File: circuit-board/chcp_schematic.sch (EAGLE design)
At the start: 18 parts, among them IC1 ATMEGA168-20P, IC2 24MAC402-SSHM-T, Q1 16 MHz

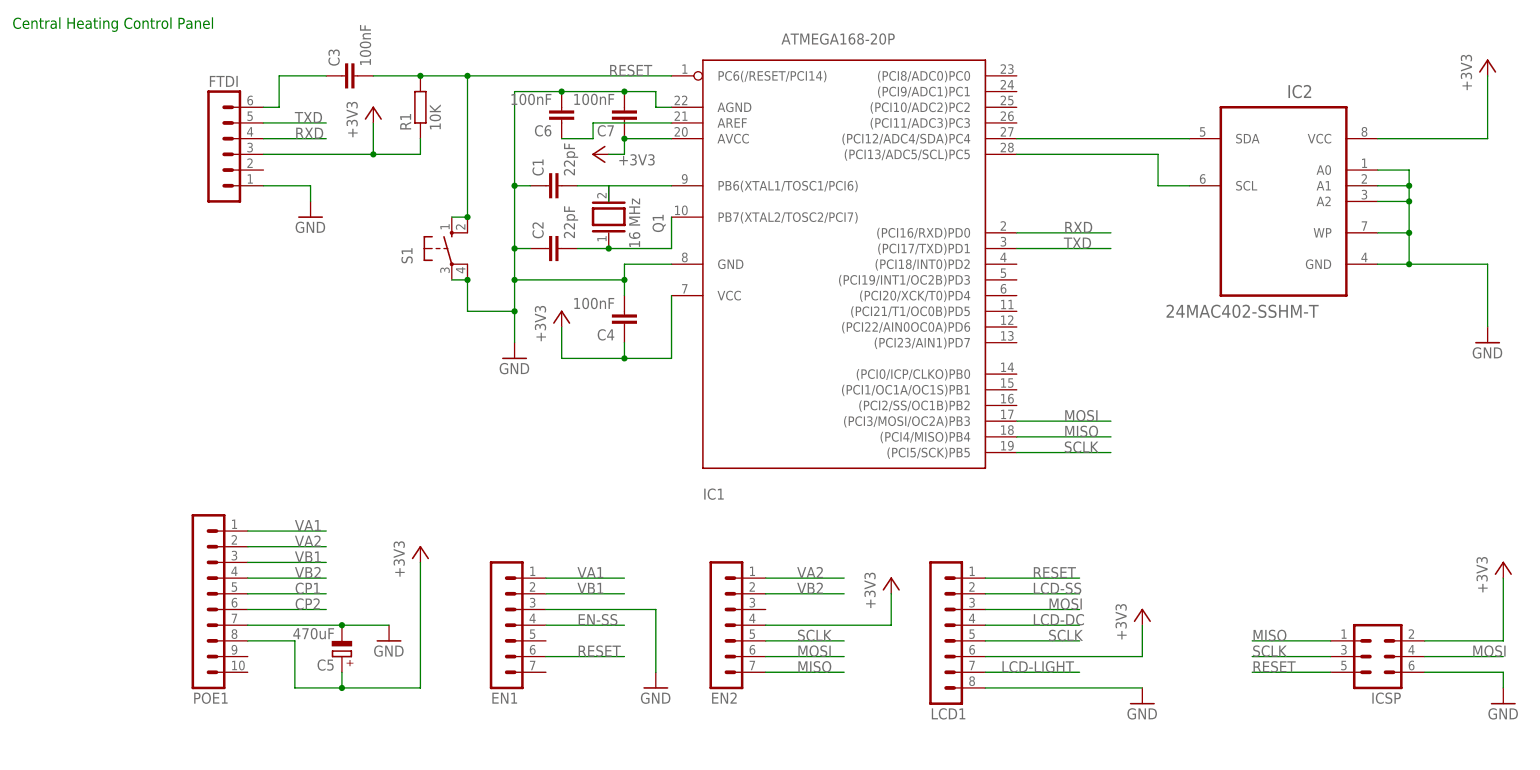
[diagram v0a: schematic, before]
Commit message: Made custom parts for the modules instead of using headers
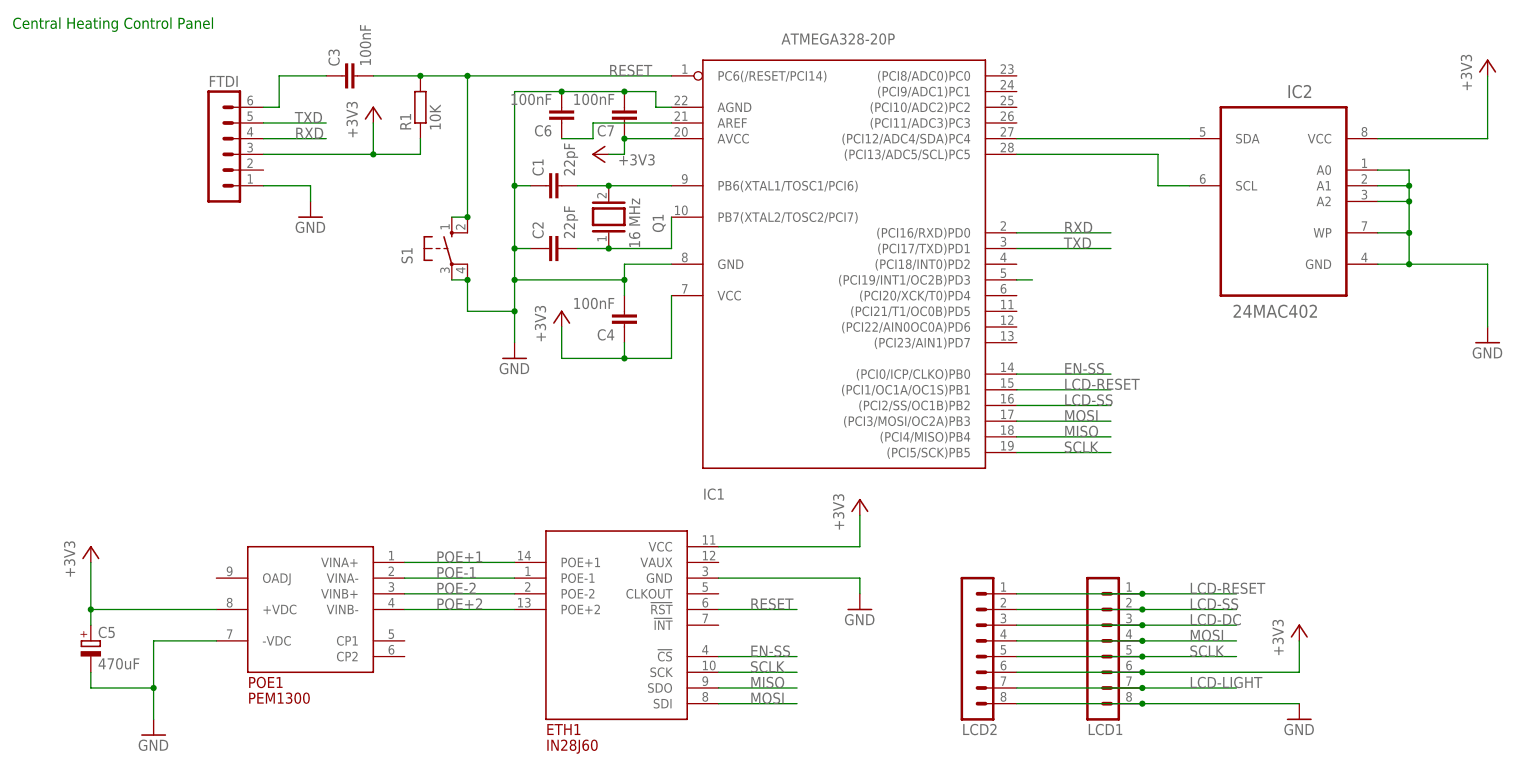
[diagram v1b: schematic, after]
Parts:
- removed EN1, EN2: (no value), con-lstb:MA07-1
- removed ICSP: (no value), con-lstb:MA03-2
- added ETH1: IN28J60, in28j60:IN28J60
- added LCD2: (no value), con-lstb:MA08-1
- IC1: value ATMEGA168-20P -> ATMEGA328-20P; device adafruit:ATMEGA168-20P -> atmega328:ATMEGA328-20P
- IC2: value 24MAC402-SSHM-T -> 24MAC402; device atmel-24mac402:24MAC402-SSHM-T -> at24mac402:24MAC402-SSHM-TPDIP
- POE1: value (none) -> PEM1300; device con-lstb:MA10-1 -> pem1300:PEM1300
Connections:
- removed net CP1: POE1.5
- removed net CP2: POE1.6
- removed net N$1 (its old number): C1.2, Q1.2
- removed net VA1: EN1.1, POE1.1
- removed net VA2: EN2.1, POE1.2
- removed net VB1: EN1.2, POE1.3
- removed net VB2: EN2.2, POE1.4
- new net LCD-RESET: IC1.(PCI1/OC1A/OC1S)PB1, LCD1.1, LCD2.1
- new net N$8: IC1.(PCI19/INT1/OC2B)PD3
- new net POE+1: ETH1.POE+1, POE1.VINA+
- new net POE+2: ETH1.POE+2, POE1.VINB-
- new net POE-1: ETH1.POE-1, POE1.VINA-
- new net POE-2: ETH1.POE-2, POE1.VINB+
- net +3V3: now also ETH1.VCC, LCD2.6, POE1.+VDC; no longer EN2.4, ICSP.2, POE1.8
- net EN-SS: now also ETH1.!CS!, IC1.(PCI0/ICP/CLKO)PB0; no longer EN1.4
- net GND: now also ETH1.GND, LCD2.8, POE1.-VDC; no longer EN1.3, ICSP.6, POE1.7
- net LCD-DC: now also LCD1.3, LCD2.3; no longer LCD1.4
- net LCD-LIGHT: now also LCD2.7
- net LCD-SS: now also IC1.(PCI2/SS/OC1B)PB2, LCD2.2
- net MISO: now also ETH1.SDO; no longer EN2.7, ICSP.1
- net MOSI: now also ETH1.SDI, LCD1.4, LCD2.4; no longer EN2.6, ICSP.4, LCD1.3
- net N$6: now also C1.2, Q1.2
- net RESET: now also ETH1.!RST!; no longer EN1.6, ICSP.5, LCD1.1
- net SCLK: now also ETH1.SCK, LCD2.5; no longer EN2.5, ICSP.3
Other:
- moved on the sheet: C5, LCD1

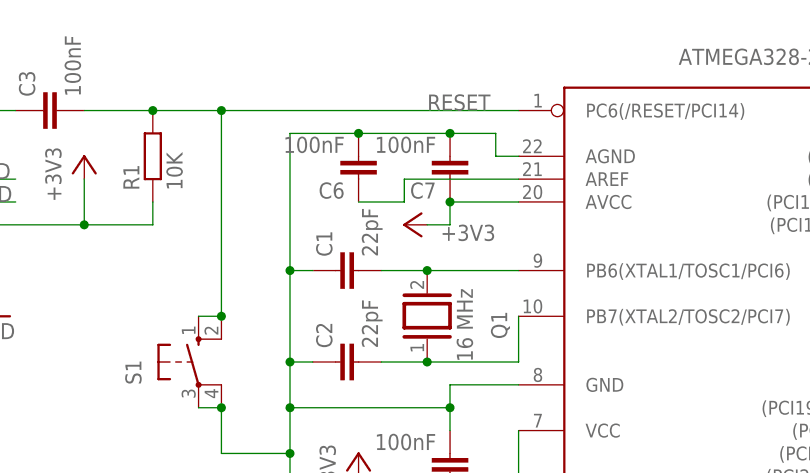
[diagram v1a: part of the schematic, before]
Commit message: Removed the unnecessary capacitor connected to AREF
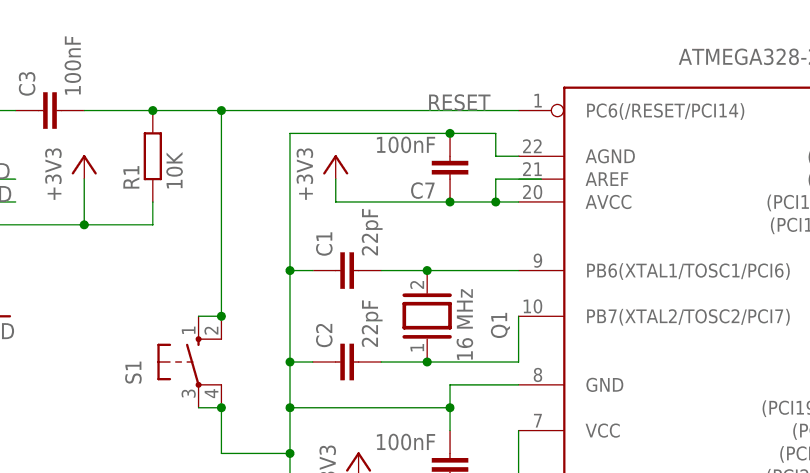
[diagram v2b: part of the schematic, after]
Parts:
- removed C6: 100nF, rcl:C-EU025-024X044
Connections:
- removed net N$7: C6.1, IC1.AREF
- net GND: no longer C6.2
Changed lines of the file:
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@@
 <part name="R1" library="rcl" deviceset="R-EU_" device="0204/7" value="10K"/>
 <part name="S1" library="switch-omron" deviceset="10-XX" device=""/>
-<part name="C6" library="rcl" deviceset="C-EU" device="025-024X044" value="100nF"/>
 <part name="C7" library="rcl" deviceset="C-EU" device="025-024X044" value="100nF"/>
 <part name="+3V8" library="supply1" deviceset="+3V3" device=""/>
@@
 <instance part="R1" gate="G$1" x="-66.04" y="55.88" rot="R90"/>
 <instance part="S1" gate="1" x="-60.96" y="33.02"/>
-<instance part="C6" gate="G$1" x="-43.18" y="53.34" rot="R180"/>
 <instance part="C7" gate="G$1" x="-33.02" y="53.34" rot="R180"/>
-<instance part="+3V8" gate="G$1" x="-38.1" y="48.26" smashed="yes" rot="R90">
-<attribute name="VALUE" x="-27.94" y="48.26" size="1.778" layer="96" rot="R180"/>
+<instance part="+3V8" gate="G$1" x="-45.72" y="55.88" smashed="yes">
+<attribute name="VALUE" x="-48.26" y="50.8" size="1.778" layer="96" rot="R90"/>
 </instance>
 <instance part="POE1" gate="G$1" x="-83.82" y="-25.4"/>
@@
 <segment>
 <pinref part="+3V8" gate="G$1" pin="+3V3"/>
-<wire x1="-35.56" y1="48.26" x2="-33.02" y2="48.26" width="0.1524" layer="91"/>
+<wire x1="-45.72" y1="53.34" x2="-45.72" y2="50.8" width="0.1524" layer="91"/>
 <pinref part="C7" gate="G$1" pin="1"/>
 <pinref part="IC1" gate="G$1" pin="AVCC"/>
-<wire x1="-25.4" y1="50.8" x2="-33.02" y2="50.8" width="0.1524" layer="91"/>
-<wire x1="-33.02" y1="48.26" x2="-33.02" y2="50.8" width="0.1524" layer="91"/>
+<wire x1="-25.4" y1="50.8" x2="-27.94" y2="50.8" width="0.1524" layer="91"/>
+<wire x1="-27.94" y1="50.8" x2="-33.02" y2="50.8" width="0.1524" layer="91"/>
+<wire x1="-45.72" y1="50.8" x2="-33.02" y2="50.8" width="0.1524" layer="91"/>
 <junction x="-33.02" y="50.8"/>
+<wire x1="-22.86" y1="53.34" x2="-27.94" y2="53.34" width="0.1524" layer="91"/>
+<wire x1="-27.94" y1="53.34" x2="-27.94" y2="50.8" width="0.1524" layer="91"/>
+<junction x="-27.94" y="50.8"/>
 </segment>
 </net>
@@
 <pinref part="GND1" gate="1" pin="GND"/>
 <wire x1="-50.8" y1="17.78" x2="-50.8" y2="22.86" width="0.1524" layer="91"/>
-<wire x1="-43.18" y1="58.42" x2="-50.8" y2="58.42" width="0.1524" layer="91"/>
 <wire x1="-50.8" y1="58.42" x2="-50.8" y2="43.18" width="0.1524" layer="91"/>
 <pinref part="C1" gate="G$1" pin="1"/>
@@
 <wire x1="-58.42" y1="22.86" x2="-50.8" y2="22.86" width="0.1524" layer="91"/>
 <junction x="-50.8" y="22.86"/>
-<pinref part="C6" gate="G$1" pin="2"/>
 <pinref part="IC1" gate="G$1" pin="AGND"/>
 <wire x1="-25.4" y1="55.88" x2="-27.94" y2="55.88" width="0.1524" layer="91"/>
 <wire x1="-27.94" y1="55.88" x2="-27.94" y2="58.42" width="0.1524" layer="91"/>
 <wire x1="-27.94" y1="58.42" x2="-33.02" y2="58.42" width="0.1524" layer="91"/>
-<junction x="-43.18" y="58.42"/>
 <pinref part="C7" gate="G$1" pin="2"/>
-<wire x1="-33.02" y1="58.42" x2="-43.18" y2="58.42" width="0.1524" layer="91"/>
+<wire x1="-33.02" y1="58.42" x2="-50.8" y2="58.42" width="0.1524" layer="91"/>
 <junction x="-33.02" y="58.42"/>
 <pinref part="C4" gate="G$1" pin="2"/>
@@
 </segment>
 </net>
-<net name="N$7" class="0">
-<segment>
-<wire x1="-38.1" y1="50.8" x2="-38.1" y2="53.34" width="0.1524" layer="91"/>
-<pinref part="IC1" gate="G$1" pin="AREF"/>
-<wire x1="-38.1" y1="53.34" x2="-25.4" y2="53.34" width="0.1524" layer="91"/>
-<wire x1="-38.1" y1="50.8" x2="-43.18" y2="50.8" width="0.1524" layer="91"/>
-<pinref part="C6" gate="G$1" pin="1"/>
-</segment>
-</net>

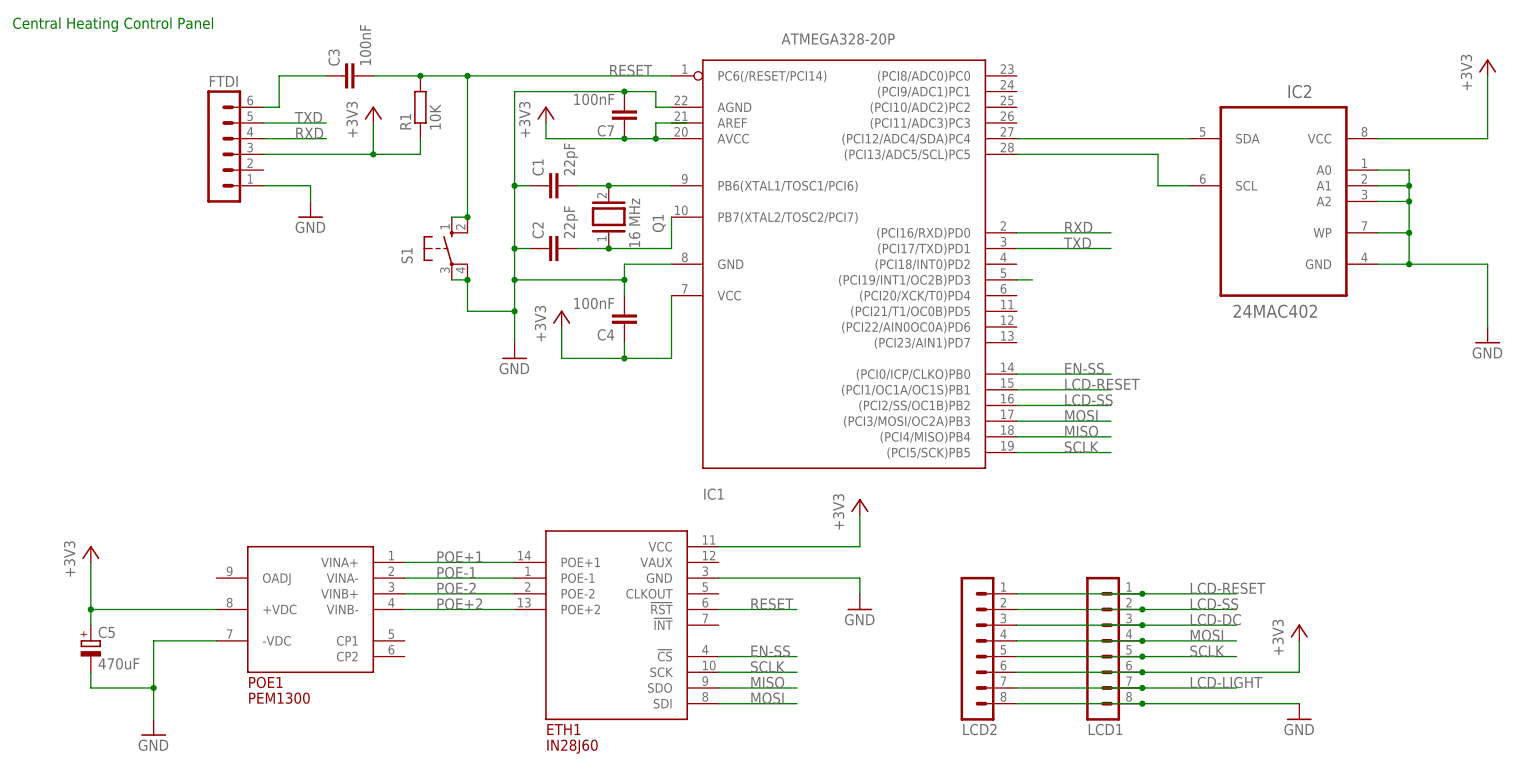
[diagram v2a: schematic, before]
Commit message: Gave jumpers both names and values
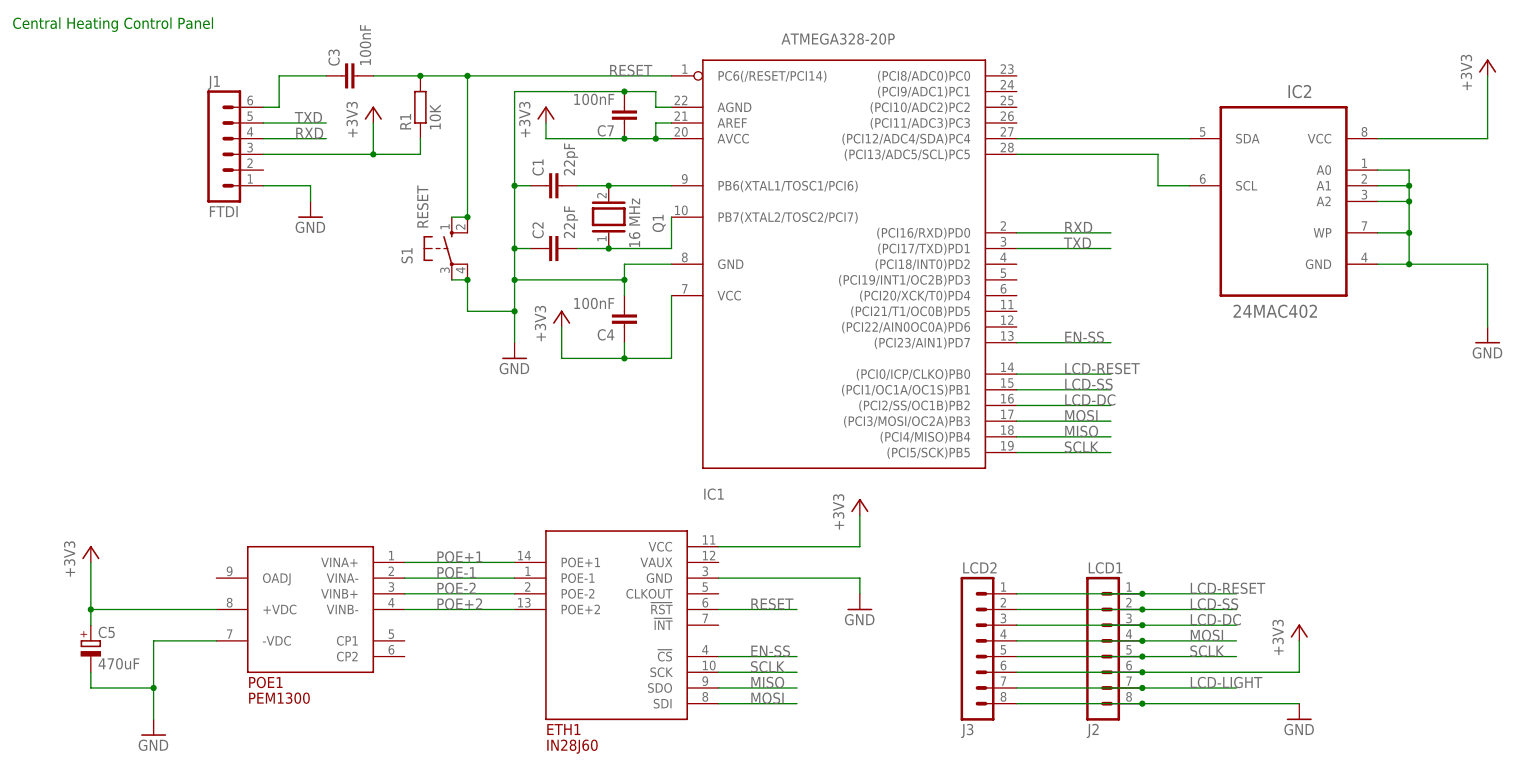
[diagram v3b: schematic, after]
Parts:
- J1: value (none) -> FTDI
- J2: value (none) -> LCD1
- J3: value (none) -> LCD2
- S1: value (none) -> RESET
- renumbered FTDI to J1, LCD1 to J2, LCD2 to J3
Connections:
- removed net N$8: IC1.(PCI19/INT1/OC2B)PD3
- net +3V3: now also IC1.AREF
- net EN-SS: now also IC1.(PCI23/AIN1)PD7; no longer IC1.(PCI0/ICP/CLKO)PB0
- net LCD-DC: now also IC1.(PCI2/SS/OC1B)PB2
- net LCD-RESET: now also IC1.(PCI0/ICP/CLKO)PB0; no longer IC1.(PCI1/OC1A/OC1S)PB1
- net LCD-SS: now also IC1.(PCI1/OC1A/OC1S)PB1; no longer IC1.(PCI2/SS/OC1B)PB2
